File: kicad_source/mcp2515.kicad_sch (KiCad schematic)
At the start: 15 parts, among them U4 MCP2515, U8 MCP2515, U9 SN65HVD232, Y1 16MHz, Y2 16MHz

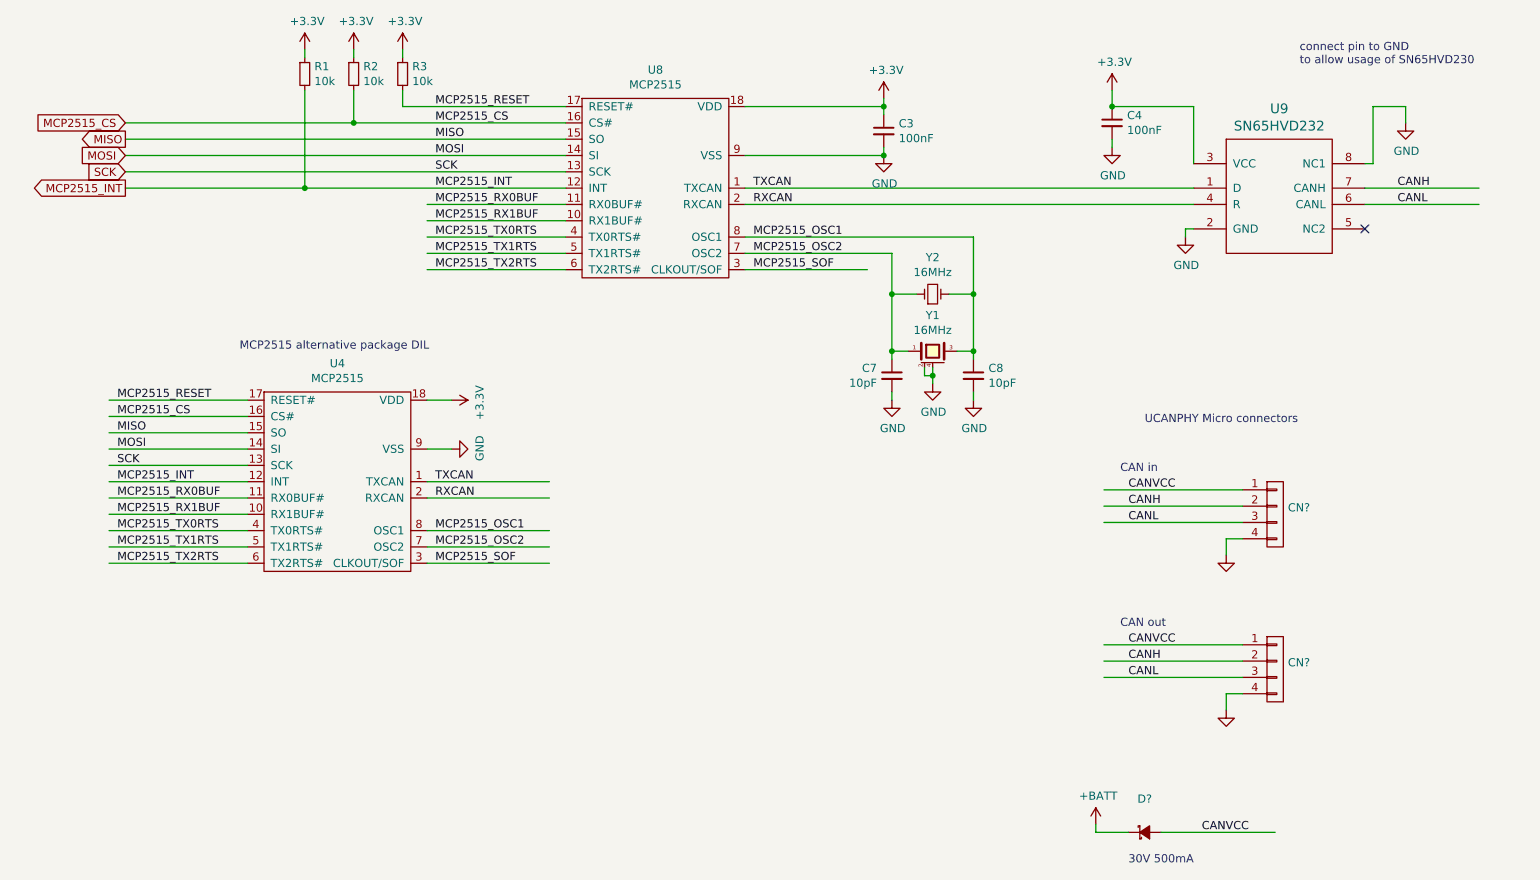
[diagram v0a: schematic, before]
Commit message: updated some symbol library links
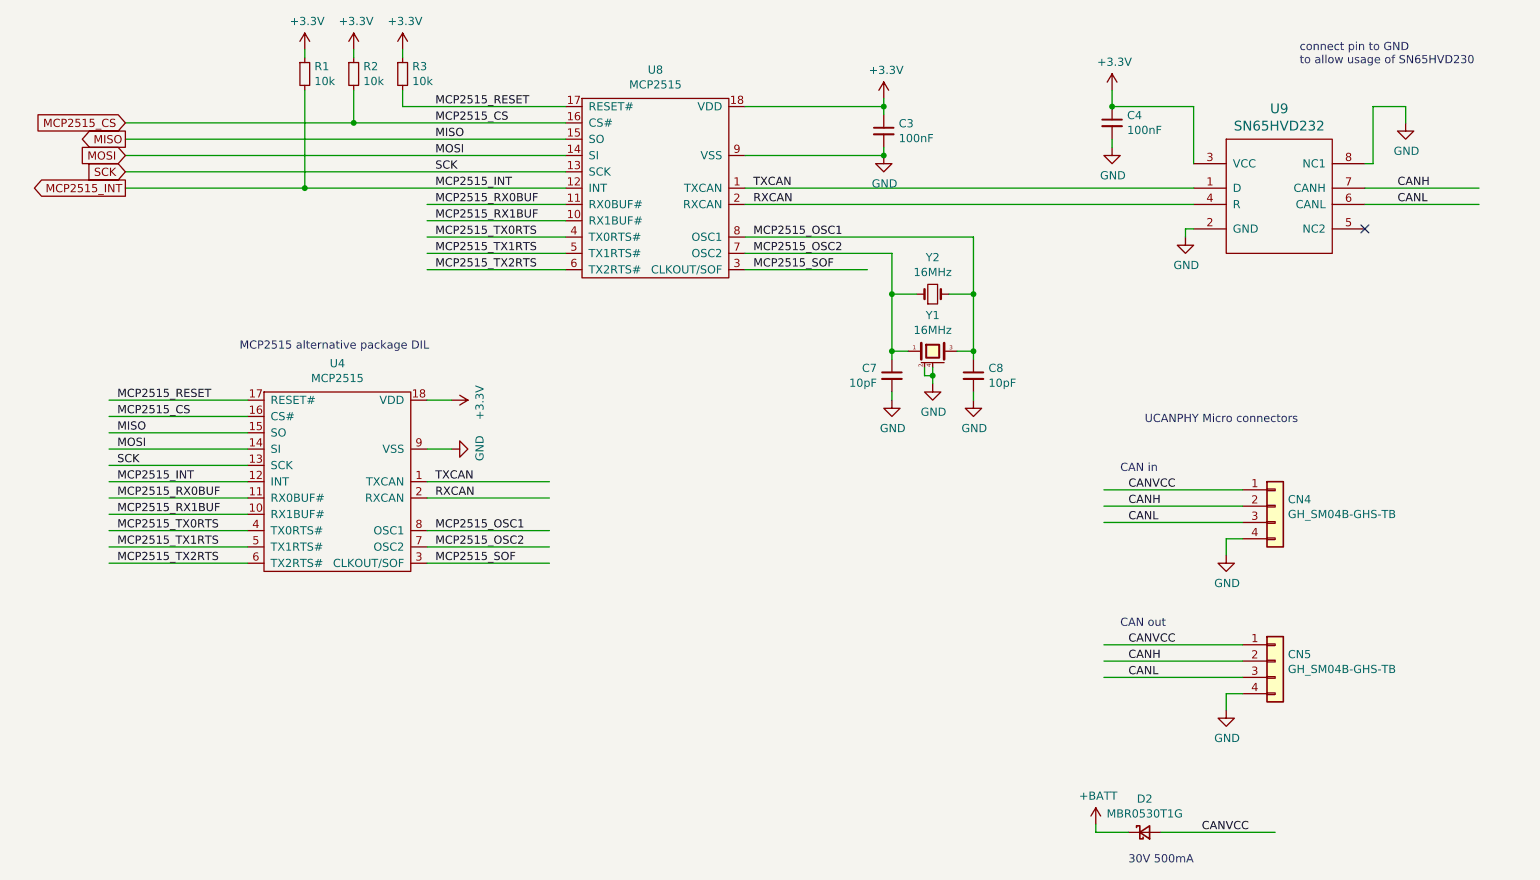
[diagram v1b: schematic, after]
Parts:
- C3, C4, C7, C8: symbol l3xz-leg-ctrl-hardware-rescue:C_0603-devices -> Device:C_Small
- CN4, CN5: renamed from CN?; value (none) -> GH_SM04B-GHS-TB; footprint (none) -> Connector_JST:JST_GH_SM04B-GHS-TB_1x04-1MP_P1.25mm_Horizontal; symbol l3xz-leg-ctrl-hardware-rescue:CONN_01X04-mechanical-connectors -> Connector_Generic:Conn_01x04
- D2: renamed from D?; value (none) -> MBR0530T1G; footprint (none) -> diodes:SOD-123; symbol l3xz-leg-ctrl-hardware-rescue:D_Schottky_Small-devices -> Device:D_Schottky_Small
- R1, R2, R3: symbol l3xz-leg-ctrl-hardware-rescue:R_0603-devices -> Device:R_Small
- Y2: symbol l3xz-leg-ctrl-hardware-rescue:Crystal_Small-devices -> Device:Crystal_Small
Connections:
- net +3V3 renamed +3.3V

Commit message: updated footprint library
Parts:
- C3, C4, C7, C8: footprint capacitors:C_0603 -> Capacitor_SMD:C_0603_1608Metric
- D2: footprint diodes:SOD-123 -> Diode_SMD:D_SOD-123
- R1, R2, R3: footprint resistors:R_0603 -> Resistor_SMD:R_0603_1608Metric
- U4: footprint DIP:DIP-18_W7.62mm -> Package_DIP:DIP-18_W7.62mm
- U8: footprint SOIC:SOIC-18_7.5x11.6mm_Pitch1.27mm -> Package_SO:SOIC-18W_7.5x11.6mm_P1.27mm
- U9: footprint SOIC:SOIC-8_3.9x4.9mm_Pitch1.27mm -> Package_SO:SOIC-8_3.9x4.9mm_P1.27mm
- Y1: footprint crystals:Crystal_SMD_3.2x2.5mm_4Pad -> Crystal:Crystal_SMD_3225-4Pin_3.2x2.5mm
- Y2: footprint crystals:HC-49V -> Crystal:Crystal_HC49-U_Vertical
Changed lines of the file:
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@@
   (title_block
     (title "l3xz-hw_leg-controller")
-    (date "2023-01-26")
+    (date "2023-01-29")
     (rev "dev_0.2")
     (company "107-systems")
@@
     (property "Reference" "U8" (id 0) (at 127 37.465 0))
     (property "Value" "MCP2515" (id 1) (at 127 39.7764 0))
-    (property "Footprint" "SOIC:SOIC-18_7.5x11.6mm_Pitch1.27mm" (id 2) (at 127 55.88 0)
+    (property "Footprint" "Package_SO:SOIC-18W_7.5x11.6mm_P1.27mm" (id 2) (at 127 55.88 0)
       (effects (font (size 1.27 1.27)) hide)
     )
@@
       (effects (font (size 1.27 1.27)) (justify left))
     )
-    (property "Footprint" "capacitors:C_0603" (id 2) (at 162.56 50.8 0)
+    (property "Footprint" "Capacitor_SMD:C_0603_1608Metric" (id 2) (at 162.56 50.8 0)
       (effects (font (size 1.27 1.27)) hide)
     )
@@
     (property "Reference" "Y1" (id 0) (at 170.18 75.692 0))
     (property "Value" "16MHz" (id 1) (at 170.18 78.0034 0))
-    (property "Footprint" "crystals:Crystal_SMD_3.2x2.5mm_4Pad" (id 2) (at 170.18 86.36 0)
+    (property "Footprint" "Crystal:Crystal_SMD_3225-4Pin_3.2x2.5mm" (id 2) (at 170.18 86.36 0)
       (effects (font (size 1.27 1.27)) hide)
     )
@@
       (effects (font (size 1.27 1.27)) (justify left))
     )
-    (property "Footprint" "resistors:R_0603" (id 2) (at 87.63 41.91 0)
+    (property "Footprint" "Resistor_SMD:R_0603_1608Metric" (id 2) (at 87.63 41.91 0)
       (effects (font (size 1.27 1.27)) hide)
     )
@@
       (effects (font (size 1.27 1.27)) (justify left))
     )
-    (property "Footprint" "resistors:R_0603" (id 2) (at 80.01 41.91 0)
+    (property "Footprint" "Resistor_SMD:R_0603_1608Metric" (id 2) (at 80.01 41.91 0)
       (effects (font (size 1.27 1.27)) hide)
     )
@@
       (effects (font (size 1.27 1.27)) (justify left))
     )
-    (property "Footprint" "resistors:R_0603" (id 2) (at 72.39 41.91 0)
+    (property "Footprint" "Resistor_SMD:R_0603_1608Metric" (id 2) (at 72.39 41.91 0)
       (effects (font (size 1.27 1.27)) hide)
     )
@@
       (effects (font (size 1.524 1.524)))
     )
-    (property "Footprint" "SOIC:SOIC-8_3.9x4.9mm_Pitch1.27mm" (id 2) (at 232.41 67.31 0)
+    (property "Footprint" "Package_SO:SOIC-8_3.9x4.9mm_P1.27mm" (id 2) (at 232.41 67.31 0)
       (effects (font (size 1.524 1.524)) hide)
     )
@@
       (effects (font (size 1.27 1.27)) (justify left))
     )
-    (property "Footprint" "capacitors:C_0603" (id 2) (at 198.12 49.53 0)
+    (property "Footprint" "Capacitor_SMD:C_0603_1608Metric" (id 2) (at 198.12 49.53 0)
       (effects (font (size 1.27 1.27)) hide)
     )
@@
     (property "Reference" "D2" (id 0) (at 203.2 151.003 0))
     (property "Value" "MBR0530T1G" (id 1) (at 203.2 153.3144 0))
-    (property "Footprint" "diodes:SOD-123" (id 2) (at 203.2 156.21 90)
+    (property "Footprint" "Diode_SMD:D_SOD-123" (id 2) (at 203.2 156.21 90)
       (effects (font (size 1.27 1.27)) hide)
     )
@@
       (effects (font (size 1.27 1.27)) (justify left))
     )
-    (property "Footprint" "capacitors:C_0603" (id 2) (at 176.53 88.9 0)
+    (property "Footprint" "Capacitor_SMD:C_0603_1608Metric" (id 2) (at 176.53 88.9 0)
       (effects (font (size 1.27 1.27)) hide)
     )
@@
       (effects (font (size 1.27 1.27)) (justify left))
     )
-    (property "Footprint" "capacitors:C_0603" (id 2) (at 163.83 88.9 0)
+    (property "Footprint" "Capacitor_SMD:C_0603_1608Metric" (id 2) (at 163.83 88.9 0)
       (effects (font (size 1.27 1.27)) hide)
     )
@@
     (property "Reference" "U4" (id 0) (at 77.47 83.185 0))
     (property "Value" "MCP2515" (id 1) (at 77.47 85.4964 0))
-    (property "Footprint" "DIP:DIP-18_W7.62mm" (id 2) (at 77.47 101.6 0)
+    (property "Footprint" "Package_DIP:DIP-18_W7.62mm" (id 2) (at 77.47 101.6 0)
       (effects (font (size 1.27 1.27)) hide)
     )
@@
     (property "Reference" "Y2" (id 0) (at 170.18 66.675 0))
     (property "Value" "16MHz" (id 1) (at 170.18 68.9864 0))
-    (property "Footprint" "crystals:HC-49V" (id 2) (at 170.18 72.39 0)
-      (effects (font (size 1.27 1.27)) hide)
-    )
+    (property "Footprint" "Crystal:Crystal_HC49-U_Vertical" (id 2) (at 170.18 72.39 0)
+      (effects (font (size 1.27 1.27)) hide)
+    )

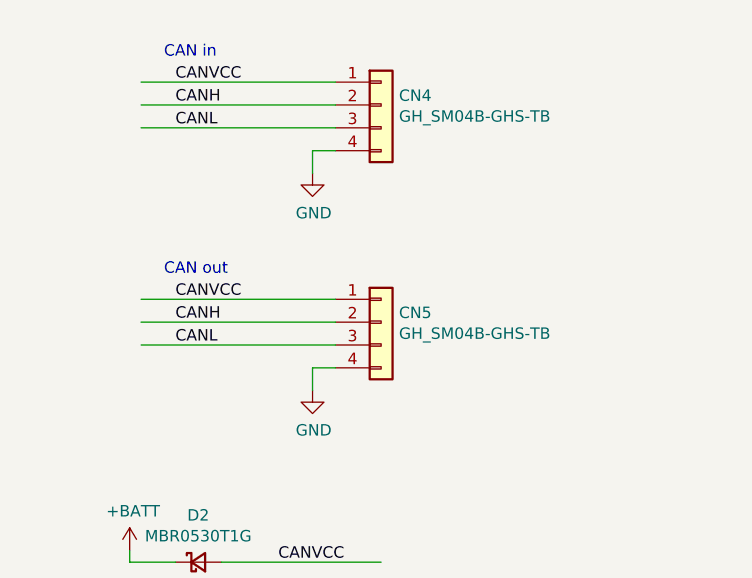
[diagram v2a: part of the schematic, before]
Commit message: connected mounting pads of connectors
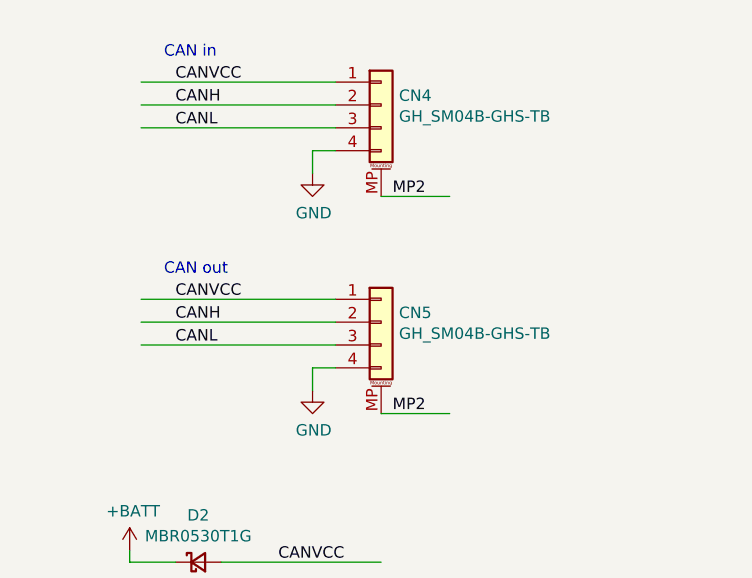
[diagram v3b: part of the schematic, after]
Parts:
- CN4, CN5: symbol Connector_Generic:Conn_01x04 -> Connector_Generic_MountingPin:Conn_01x04_MountingPin
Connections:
- new net MP2: CN4.MP (MountPin), CN5.MP (MountPin)
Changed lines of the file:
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@@
+    (stroke (width 0) (type default) (color 0 0 0 0))
+  )
+  (wire (pts (xy 223.52 115.57) (xy 231.14 115.57))
     (stroke (width 0) (type default) (color 0 0 0 0))
   )
@@
     (stroke (width 0) (type default) (color 0 0 0 0))
   )
+  (wire (pts (xy 223.52 139.7) (xy 231.14 139.7))
+    (stroke (width 0) (type default) (color 0 0 0 0))
+  )
   (wire (pts (xy 218.44 110.49) (xy 215.9 110.49))
     (stroke (width 0) (type default) (color 0 0 0 0))
@@
     (effects (font (size 1.27 1.27)) (justify left bottom))
   )
+  (label "MP2" (at 224.79 139.7 0)
+    (effects (font (size 1.27 1.27)) (justify left bottom))
+  )
   (label "SCK" (at 92.71 53.34 0)
     (effects (font (size 1.27 1.27)) (justify left bottom))
@@
   )
   (label "SCK" (at 43.18 99.06 0)
+    (effects (font (size 1.27 1.27)) (justify left bottom))
+  )
+  (label "MP2" (at 224.79 115.57 0)
     (effects (font (size 1.27 1.27)) (justify left bottom))
   )
@@
     (pin "1")
   )
-  (symbol (lib_id "Connector_Generic:Conn_01x04") (at 223.52 105.41 0) (unit 1)
+  (symbol (lib_id "Connector_Generic_MountingPin:Conn_01x04_MountingPin") (at 223.52 105.41 0) (unit 1)
     (in_bom yes) (on_board yes)
     (property "Reference" "CN4" (id 0) (at 225.5012 104.3686 0)
@@
       (effects (font (size 1.27 1.27)) hide)
     )
-    (property "Datasheet" "" (id 3) (at 223.52 105.41 0))
+    (property "Datasheet" "~" (id 3) (at 223.52 105.41 0)
+      (effects (font (size 1.27 1.27)) hide)
+    )
     (pin "1")
     (pin "2")
     (pin "3")
     (pin "4")
+    (pin "MP")
   )
   (symbol (lib_id "power:GND") (at 215.9 113.03 0) (unit 1)
@@
     (pin "1")
   )
-  (symbol (lib_id "Connector_Generic:Conn_01x04") (at 223.52 129.54 0) (unit 1)
+  (symbol (lib_id "Connector_Generic_MountingPin:Conn_01x04_MountingPin") (at 223.52 129.54 0) (unit 1)
     (in_bom yes) (on_board yes)
     (property "Reference" "CN5" (id 0) (at 225.5012 128.4986 0)
@@
       (effects (font (size 1.27 1.27)) hide)
     )
-    (property "Datasheet" "" (id 3) (at 223.52 129.54 0))
+    (property "Datasheet" "~" (id 3) (at 223.52 129.54 0)
+      (effects (font (size 1.27 1.27)) hide)
+    )
     (pin "1")
     (pin "2")
     (pin "3")
     (pin "4")
+    (pin "MP")
   )
   (symbol (lib_id "power:GND") (at 215.9 137.16 0) (unit 1)

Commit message: fixed drc errors
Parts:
- Y1: footprint Crystal:Crystal_SMD_3225-4Pin_3.2x2.5mm -> Crystal:Crystal_SMD_SeikoEpson_FA238V-4Pin_3.2x2.5mm
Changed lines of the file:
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@@
     (property "Reference" "Y1" (id 0) (at 170.18 75.692 0))
     (property "Value" "16MHz" (id 1) (at 170.18 78.0034 0))
-    (property "Footprint" "Crystal:Crystal_SMD_3225-4Pin_3.2x2.5mm" (id 2) (at 170.18 86.36 0)
+    (property "Footprint" "Crystal:Crystal_SMD_SeikoEpson_FA238V-4Pin_3.2x2.5mm" (id 2) (at 170.18 86.36 0)
       (effects (font (size 1.27 1.27)) hide)
     )
